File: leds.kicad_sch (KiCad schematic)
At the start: 11 parts, among them IC1 STPIC6D595TTR, IC2 STPIC6D595TTR, IC3 STPIC6D595TTR, IC4 STPIC6D595TTR, IC5 STPIC6D595TTR

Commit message: New template
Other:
- company: (none) -> STAPsystem
- title: (none) -> RPM meter LED
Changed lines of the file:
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@@
 	(generator_version "8.0")
 	(paper "A3")
+	(title_block
+		(title "RPM meter LED")
+		(date "2024-11-26")
+		(rev "v1.0")
+		(company "STAPsystem")
+	)
 	(wire
 		(pts

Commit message: ws2812b
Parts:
- removed C17, C18, C19, C20, C21: 100n, Capacitor_SMD:C_0603_1608Metric, symbol Device:C_Small
- removed IC1, IC2, IC3, IC4, IC5: STPIC6D595TTR, Library_local:SOP65P640X120-16N, symbol local_library:STPIC6D595TTR
- removed R8: 10k, Resistor_SMD:R_0603_1608Metric, symbol Device:R
- added D10, D11, D12, D13, D14, D15, D16, D17, D18, D19, D20, D21, D22, D3, D4, D5, D6, D7, D8, D9: WS2812B, LED_SMD:LED_WS2812B_PLCC4_5.0x5.0mm_P3.2mm, symbol LED:WS2812B
- added IC1: SN74LV1T34DCKR, Library_local:SOT65P210X110-5N, symbol local_library:SN74LV1T34DCKR
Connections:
- net +5V: now also D10.1 (VDD), D11.1 (VDD), D12.1 (VDD), D13.1 (VDD), D14.1 (VDD), D15.1 (VDD), D16.1 (VDD), D17.1 (VDD), D18.1 (VDD), D19.1 (VDD), D20.1 (VDD), D21.1 (VDD), D22.1 (VDD), D3.1 (VDD), D4.1 (VDD), D5.1 (VDD), D6.1 (VDD), D7.1 (VDD), D8.1 (VDD), D9.1 (VDD), IC1.5 (VCC)
- net GND: now also D10.3 (VSS), D11.3 (VSS), D12.3 (VSS), D13.3 (VSS), D14.3 (VSS), D15.3 (VSS), D16.3 (VSS), D17.3 (VSS), D18.3 (VSS), D19.3 (VSS), D20.3 (VSS), D21.3 (VSS), D22.3 (VSS), D3.3 (VSS), D4.3 (VSS), D5.3 (VSS), D6.3 (VSS), D7.3 (VSS), D8.3 (VSS), D9.3 (VSS), IC1.3 (GND)
- new net: D7.2 (DOUT), D8.4 (DIN)
- new net: D6.2 (DOUT), D7.4 (DIN)
- new net: D10.2 (DOUT), D11.4 (DIN)
- new net: D10.4 (DIN), D9.2 (DOUT)
- new net: D14.2 (DOUT), D15.4 (DIN)
- new net: D13.2 (DOUT), D14.4 (DIN)
- new net: D18.2 (DOUT), D19.4 (DIN)
- new net: D17.2 (DOUT), D18.4 (DIN)
- new net: D16.2 (DOUT), D17.4 (DIN)
- new net: D15.2 (DOUT), D16.4 (DIN)
- new net: D8.2 (DOUT), D9.4 (DIN)
- new net: D11.2 (DOUT), D12.4 (DIN)
- new net: D21.2 (DOUT), D22.4 (DIN)
- new net: D4.2 (DOUT), D5.4 (DIN)
- new net: D3.2 (DOUT), D4.4 (DIN)
- new net: D3.4 (DIN), IC1.4 (Y)
- new net: D12.2 (DOUT), D13.4 (DIN)
- new net: D19.2 (DOUT), D20.4 (DIN)
- new net: D5.2 (DOUT), D6.4 (DIN)
- new net: D20.2 (DOUT), D21.4 (DIN)
- new net WS2812B_IN: IC1.2 (A)
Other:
- removed sheet led_segment0
- removed sheet led_segment1
- removed sheet led_segment10
- removed sheet led_segment11
- removed sheet led_segment12
- removed sheet led_segment13
- removed sheet led_segment14
- removed sheet led_segment15
- removed sheet led_segment16
- removed sheet led_segment17
- removed sheet led_segment18
- removed sheet led_segment19
- removed sheet led_segment2
- removed sheet led_segment3
- removed sheet led_segment4
- removed sheet led_segment5
- removed sheet led_segment6
- removed sheet led_segment7
- removed sheet led_segment8
- removed sheet led_segment9
- note added: "LED0"
- note added: "LED19"

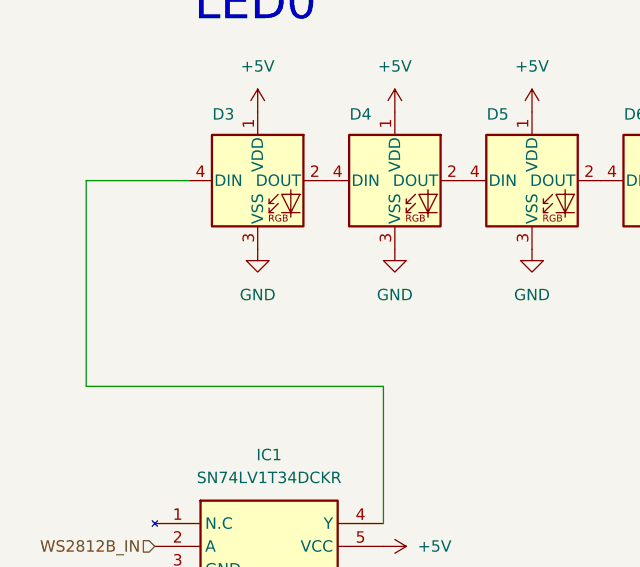
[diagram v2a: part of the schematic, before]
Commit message: TVS protection
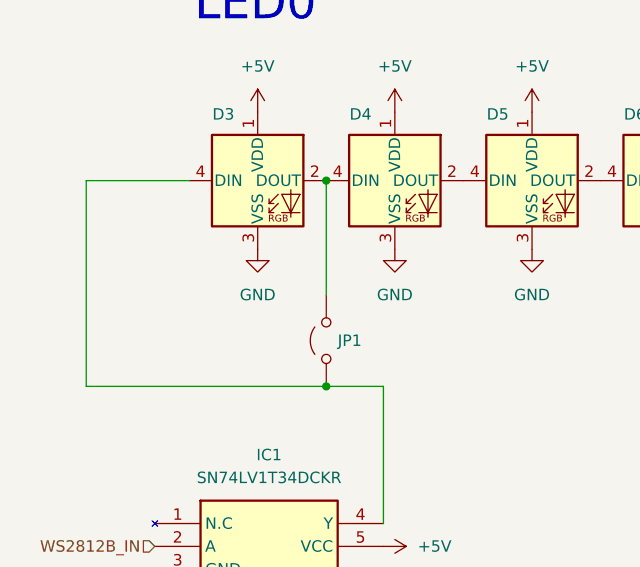
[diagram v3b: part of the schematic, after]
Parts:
- added JP1: Jumper_2_Open, Jumper:SolderJumper-2_P1.3mm_Open_TrianglePad1.0x1.5mm, symbol Jumper:Jumper_2_Open
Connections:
- net at D3.2 (DOUT), D4.4 (DIN): now also JP1.2 (B)
- net at D3.4 (DIN), IC1.4 (Y): now also JP1.1 (A)
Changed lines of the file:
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@@
 		(company "STAPsystem")
+	)
+	(junction
+		(at 80.01 130.81)
+		(diameter 0)
+		(color 0 0 0 0)
+	)
+	(junction
+		(at 80.01 107.95)
+		(diameter 0)
+		(color 0 0 0 0)
 	)
 	(wire
 		(pts
-			(xy 86.36 130.81) (xy 53.34 130.81)
+			(xy 86.36 130.81) (xy 80.01 130.81)
 		)
 		(stroke
@@
 	(wire
 		(pts
+			(xy 80.01 107.95) (xy 80.01 120.65)
+		)
+		(stroke
+			(width 0)
+			(type default)
+		)
+	)
+	(wire
+		(pts
 			(xy 86.36 146.05) (xy 86.36 130.81)
+		)
+		(stroke
+			(width 0)
+			(type default)
+		)
+	)
+	(wire
+		(pts
+			(xy 80.01 130.81) (xy 53.34 130.81)
 		)
 		(stroke
@@
 					(unit 1)
 				)
+			)
+		)
+	)
+	(symbol
+		(lib_id "Jumper:Jumper_2_Open")
+		(at 80.01 125.73 90)
+		(unit 1)
+		(exclude_from_sim yes)
+		(in_bom yes)
+		(on_board yes)
+		(dnp no)
+		(fields_autoplaced yes)
+		(property "Reference" "JP1"
+			(at 81.28 125.7299 90)
+			(effects
+				(font
+					(size 1.27 1.27)
+				)
+				(justify right)
+			)
+		)
+		(property "Value" "Jumper_2_Open"
+			(at 81.28 126.9999 90)
+			(effects
+				(font
+					(size 1.27 1.27)
+				)
+				(justify right)
+				(hide yes)
+			)
+		)
+		(property "Footprint" "Jumper:SolderJumper-2_P1.3mm_Open_TrianglePad1.0x1.5mm"
+			(at 80.01 125.73 0)
+			(effects
+				(font
+					(size 1.27 1.27)
+				)
+				(hide yes)
+			)
+		)
+		(property "Datasheet" "~"
+			(at 80.01 125.73 0)
+			(effects
+				(font
+					(size 1.27 1.27)
+				)
+				(hide yes)
+			)
+		)
+		(property "Description" "Jumper, 2-pole, open"
+			(at 80.01 125.73 0)
+			(effects
+				(font
+					(size 1.27 1.27)
+				)
+				(hide yes)
+			)
+		)
+		(pin "2"
+		)
+		(pin "1"
+		)
+		(instances
+			(project ""
+				(path "/c95b12ac-441d-4f7a-bd6a-c2e5d81eb286/45a986c6-70d0-42c7-9293-21dd4ecec7b9"
+					(reference "JP1")
+					(unit 1)
+				)

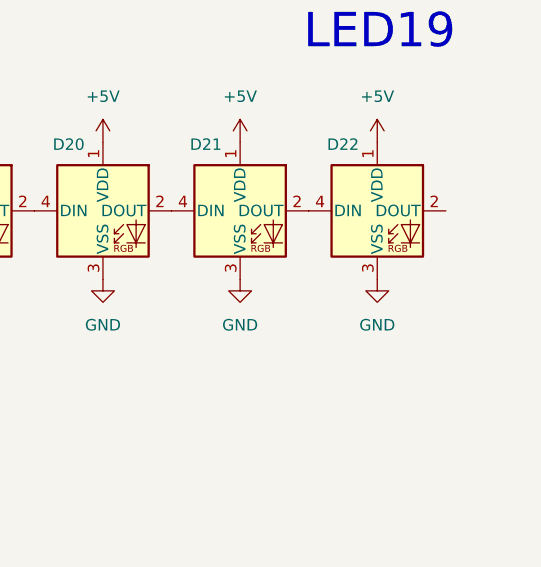
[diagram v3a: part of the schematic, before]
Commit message: Add optional leds end resistors
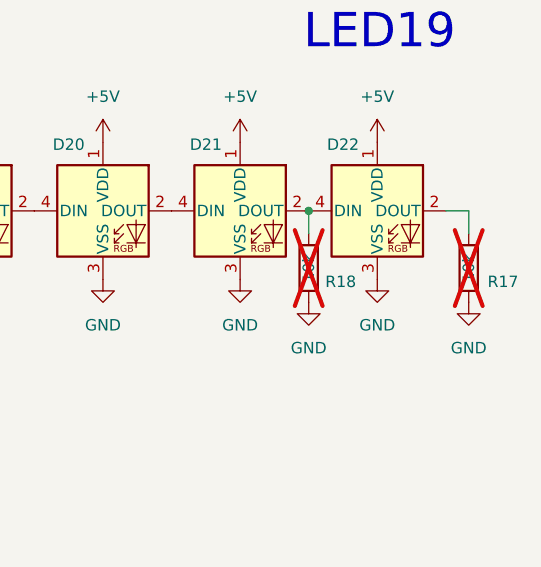
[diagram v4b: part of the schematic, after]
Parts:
- added R17, R18: 10k, Resistor_SMD:R_0603_1608Metric, symbol Device:R
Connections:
- net GND: now also R17.1, R18.1
- net at D22.2 (DOUT): now also R17.2
- net at D21.2 (DOUT), D22.4 (DIN): now also R18.2

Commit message: 2.1
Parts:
- added C21, C29, C30, C31, C32, C33, C34, C35, C36, C37, C38, C39, C40, C41, C42, C43, C44, C45, C46, C47: 100n, Capacitor_SMD:C_0603_1608Metric, symbol Device:C_Small
- D10, D11, D12, D13, D14, D15, D16, D17, D18, D19, D20, D21, D22, D3, D4, D5, D6, D7, D8, D9: footprint LED_SMD:LED_WS2812B_PLCC4_5.0x5.0mm_P3.2mm -> Library_local:LED_WS2812B-2020_PLCC4_2.0x2.0mm
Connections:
- net +5V: now also C21.1, C29.1, C30.1, C31.1, C32.1, C33.1, C34.1, C35.1, C36.1, C37.1, C38.1, C39.1, C40.1, C41.1, C42.1, C43.1, C44.1, C45.1, C46.1, C47.1
- net GND: now also C21.2, C29.2, C30.2, C31.2, C32.2, C33.2, C34.2, C35.2, C36.2, C37.2, C38.2, C39.2, C40.2, C41.2, C42.2, C43.2, C44.2, C45.2, C46.2, C47.2
